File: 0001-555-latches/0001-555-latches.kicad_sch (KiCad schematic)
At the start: 33 parts, among them J1 DC_IN, J2 ASTBL_OUT, J3 BSTBL_OUT, J4 MSTBL_OUT, SW1 SW_Push, SW2 SW_Push, SW3 SW_Push, U1 NE555P, U2 NE555P, U3 NE555P

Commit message: footprints
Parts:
- C1, C2, C3, C5: footprint (none) -> Capacitor_THT:C_Rect_L7.0mm_W3.5mm_P5.00mm
- C4: footprint (none) -> Capacitor_THT:CP_Radial_D5.0mm_P2.00mm
- D1, D2, D3: footprint (none) -> LED_THT:LED_D5.0mm
- J1, J2, J3, J4: footprint (none) -> TerminalBlock_MetzConnect:TerminalBlock_MetzConnect_Type059_RT06302HBWC_1x02_P3.50mm_Horizontal
- R1, R10, R11, R12, R2, R3, R4, R5, R6, R7, R8, R9: footprint (none) -> Resistor_THT:R_Axial_DIN0207_L6.3mm_D2.5mm_P7.62mm_Horizontal
- RV1, RV2, RV3: footprint (none) -> Potentiometer_THT:Potentiometer_Runtron_RM-065_Vertical
- SW1, SW2, SW3: footprint (none) -> Button_Switch_THT:SW_PUSH_6mm_H4.3mm
- U1, U2, U3: footprint (none) -> Package_DIP:DIP-8_W7.62mm_Socket_LongPads
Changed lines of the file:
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@@
 			)
 		)
-		(property "Footprint" ""
+		(property "Footprint" "Button_Switch_THT:SW_PUSH_6mm_H4.3mm"
 			(at 116.84 76.2 0)
 			(effects
@@
 			)
 		)
-		(property "Footprint" ""
+		(property "Footprint" "LED_THT:LED_D5.0mm"
 			(at 78.74 92.71 0)
 			(effects
@@
 			)
 		)
-		(property "Footprint" ""
+		(property "Footprint" "Capacitor_THT:C_Rect_L7.0mm_W3.5mm_P5.00mm"
 			(at 135.5852 99.06 0)
 			(effects
@@
 			)
 		)
-		(property "Footprint" ""
+		(property "Footprint" "Resistor_THT:R_Axial_DIN0207_L6.3mm_D2.5mm_P7.62mm_Horizontal"
 			(at 132.842 34.29 90)
 			(effects
@@
 			)
 		)
-		(property "Footprint" ""
+		(property "Footprint" "Resistor_THT:R_Axial_DIN0207_L6.3mm_D2.5mm_P7.62mm_Horizontal"
 			(at 85.09 72.898 90)
 			(effects
@@
 			)
 		)
-		(property "Footprint" ""
+		(property "Footprint" "Resistor_THT:R_Axial_DIN0207_L6.3mm_D2.5mm_P7.62mm_Horizontal"
 			(at 196.342 34.29 90)
 			(effects
@@
 			)
 		)
-		(property "Footprint" ""
+		(property "Footprint" "Capacitor_THT:C_Rect_L7.0mm_W3.5mm_P5.00mm"
 			(at 211.7852 99.06 0)
 			(effects
@@
 			)
 		)
-		(property "Footprint" ""
+		(property "Footprint" "TerminalBlock_MetzConnect:TerminalBlock_MetzConnect_Type059_RT06302HBWC_1x02_P3.50mm_Horizontal"
 			(at 116.84 134.62 0)
 			(effects
@@
 			)
 		)
-		(property "Footprint" ""
+		(property "Footprint" "Package_DIP:DIP-8_W7.62mm_Socket_LongPads"
 			(at 74.93 86.36 0)
 			(effects
@@
 			)
 		)
-		(property "Footprint" ""
+		(property "Footprint" "Resistor_THT:R_Axial_DIN0207_L6.3mm_D2.5mm_P7.62mm_Horizontal"
 			(at 252.222 80.01 90)
 			(effects
@@
 			)
 		)
-		(property "Footprint" ""
+		(property "Footprint" "Button_Switch_THT:SW_PUSH_6mm_H4.3mm"
 			(at 116.84 53.34 0)
 			(effects
@@
 			)
 		)
-		(property "Footprint" ""
+		(property "Footprint" "Capacitor_THT:C_Rect_L7.0mm_W3.5mm_P5.00mm"
 			(at 39.0652 99.06 0)
 			(effects
@@
 			)
 		)
-		(property "Footprint" ""
+		(property "Footprint" "Resistor_THT:R_Axial_DIN0207_L6.3mm_D2.5mm_P7.62mm_Horizontal"
 			(at 239.522 34.29 90)
 			(effects
@@
 			)
 		)
-		(property "Datasheet" "~"
+		(property "Datasheet" ""
 			(at 241.3 34.29 0)
 			(effects
@@
 			)
 		)
-		(property "Footprint" ""
+		(property "Footprint" "Potentiometer_THT:Potentiometer_Runtron_RM-065_Vertical"
 			(at 241.3 46.99 0)
 			(effects
@@
 			)
 		)
-		(property "Footprint" ""
+		(property "Footprint" "Package_DIP:DIP-8_W7.62mm_Socket_LongPads"
 			(at 166.37 86.36 0)
 			(effects
@@
 			)
 		)
-		(property "Footprint" ""
+		(property "Footprint" "Button_Switch_THT:SW_PUSH_6mm_H4.3mm"
 			(at 193.04 81.28 0)
 			(effects
@@
 			)
 		)
-		(property "Footprint" ""
+		(property "Footprint" "Resistor_THT:R_Axial_DIN0207_L6.3mm_D2.5mm_P7.62mm_Horizontal"
 			(at 173.99 72.898 90)
 			(effects
@@
 			)
 		)
-		(property "Footprint" ""
+		(property "Footprint" "Potentiometer_THT:Potentiometer_Runtron_RM-065_Vertical"
 			(at 27.94 52.07 0)
 			(effects
@@
 			)
 		)
-		(property "Footprint" ""
+		(property "Footprint" "Package_DIP:DIP-8_W7.62mm_Socket_LongPads"
 			(at 242.57 86.36 0)
 			(effects
@@
 			)
 		)
-		(property "Footprint" ""
+		(property "Footprint" "TerminalBlock_MetzConnect:TerminalBlock_MetzConnect_Type059_RT06302HBWC_1x02_P3.50mm_Horizontal"
 			(at 157.48 134.62 0)
 			(effects
@@
 			)
 		)
-		(property "Footprint" ""
+		(property "Footprint" "Resistor_THT:R_Axial_DIN0207_L6.3mm_D2.5mm_P7.62mm_Horizontal"
 			(at 122.682 34.29 90)
 			(effects
@@
 			)
 		)
-		(property "Footprint" ""
+		(property "Footprint" "Capacitor_THT:C_Rect_L7.0mm_W3.5mm_P5.00mm"
 			(at 28.9052 99.06 0)
 			(effects
@@
 			)
 		)
-		(property "Footprint" ""
+		(property "Footprint" "Capacitor_THT:CP_Radial_D5.0mm_P2.00mm"
 			(at 242.2652 99.06 0)
 			(effects
@@
 			)
 		)
-		(property "Footprint" ""
+		(property "Footprint" "TerminalBlock_MetzConnect:TerminalBlock_MetzConnect_Type059_RT06302HBWC_1x02_P3.50mm_Horizontal"
 			(at 40.64 134.62 0)
 			(effects
@@
 			)
 		)
-		(property "Footprint" ""
+		(property "Footprint" "TerminalBlock_MetzConnect:TerminalBlock_MetzConnect_Type059_RT06302HBWC_1x02_P3.50mm_Horizontal"
 			(at 76.2 134.62 0)
 			(effects
@@
 			)
 		)
-		(property "Footprint" ""
+		(property "Footprint" "Resistor_THT:R_Axial_DIN0207_L6.3mm_D2.5mm_P7.62mm_Horizontal"
 			(at 76.962 80.01 90)
 			(effects
@@
 			)
 		)
-		(property "Footprint" ""
+		(property "Footprint" "LED_THT:LED_D5.0mm"
 			(at 254 92.71 0)
 			(effects
@@
 			)
 		)
-		(property "Footprint" ""
+		(property "Footprint" "Resistor_THT:R_Axial_DIN0207_L6.3mm_D2.5mm_P7.62mm_Horizontal"
 			(at 26.162 29.21 90)
 			(effects
@@
 			)
 		)
-		(property "Footprint" ""
+		(property "Footprint" "Potentiometer_THT:Potentiometer_Runtron_RM-065_Vertical"
 			(at 27.94 39.37 0)
 			(effects
@@
 			)
 		)
-		(property "Footprint" ""
+		(property "Footprint" "LED_THT:LED_D5.0mm"
 			(at 167.64 92.71 0)
 			(effects
@@
 			)
 		)
-		(property "Footprint" ""
+		(property "Footprint" "Resistor_THT:R_Axial_DIN0207_L6.3mm_D2.5mm_P7.62mm_Horizontal"
 			(at 260.35 72.898 90)
 			(effects
@@
 			)
 		)
-		(property "Footprint" ""
+		(property "Footprint" "Resistor_THT:R_Axial_DIN0207_L6.3mm_D2.5mm_P7.62mm_Horizontal"
 			(at 26.162 64.77 90)
 			(effects
@@
 			)
 		)
-		(property "Footprint" ""
+		(property "Footprint" "Resistor_THT:R_Axial_DIN0207_L6.3mm_D2.5mm_P7.62mm_Horizontal"
 			(at 165.862 80.01 90)
 			(effects

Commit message: Fix typo
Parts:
- D3: value YELLO -> YELLOW
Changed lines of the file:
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@@
 			)
 		)
-		(property "Value" "YELLO"
+		(property "Value" "YELLOW"
 			(at 257.81 95.5674 90)
 			(effects

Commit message: First PCB drafts
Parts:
- J1, J2, J3, J4: footprint TerminalBlock_MetzConnect:TerminalBlock_MetzConnect_Type059_RT06302HBWC_1x02_P3.50mm_Horizontal -> TerminalBlock_4Ucon:TerminalBlock_4Ucon_1x02_P3.50mm_Horizontal
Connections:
- net at R6.2: now also RV3.3; no longer RV3.1
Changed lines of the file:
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@@
 			)
 		)
-		(property "Footprint" "TerminalBlock_MetzConnect:TerminalBlock_MetzConnect_Type059_RT06302HBWC_1x02_P3.50mm_Horizontal"
+		(property "Footprint" "TerminalBlock_4Ucon:TerminalBlock_4Ucon_1x02_P3.50mm_Horizontal"
 			(at 116.84 134.62 0)
 			(effects
@@
 		(lib_id "Device:R_Potentiometer")
 		(at 241.3 46.99 0)
-		(unit 1)
-		(exclude_from_sim no)
-		(in_bom yes)
-		(on_board yes)
-		(dnp no)
-		(fields_autoplaced yes)
+		(mirror x)
+		(unit 1)
+		(exclude_from_sim no)
+		(in_bom yes)
+		(on_board yes)
+		(dnp no)
 		(property "Reference" "RV3"
-			(at 238.76 45.7199 0)
+			(at 238.76 48.2601 0)
 			(effects
 				(font
@@
 		)
 		(property "Value" "1M"
-			(at 238.76 48.2599 0)
+			(at 238.76 45.7201 0)
 			(effects
 				(font
@@
 			)
 		)
-		(property "Footprint" "TerminalBlock_MetzConnect:TerminalBlock_MetzConnect_Type059_RT06302HBWC_1x02_P3.50mm_Horizontal"
+		(property "Footprint" "TerminalBlock_4Ucon:TerminalBlock_4Ucon_1x02_P3.50mm_Horizontal"
 			(at 157.48 134.62 0)
 			(effects
@@
 			)
 		)
-		(property "Footprint" "TerminalBlock_MetzConnect:TerminalBlock_MetzConnect_Type059_RT06302HBWC_1x02_P3.50mm_Horizontal"
+		(property "Footprint" "TerminalBlock_4Ucon:TerminalBlock_4Ucon_1x02_P3.50mm_Horizontal"
 			(at 40.64 134.62 0)
 			(effects
@@
 			)
 		)
-		(property "Footprint" "TerminalBlock_MetzConnect:TerminalBlock_MetzConnect_Type059_RT06302HBWC_1x02_P3.50mm_Horizontal"
+		(property "Footprint" "TerminalBlock_4Ucon:TerminalBlock_4Ucon_1x02_P3.50mm_Horizontal"
 			(at 76.2 134.62 0)
 			(effects

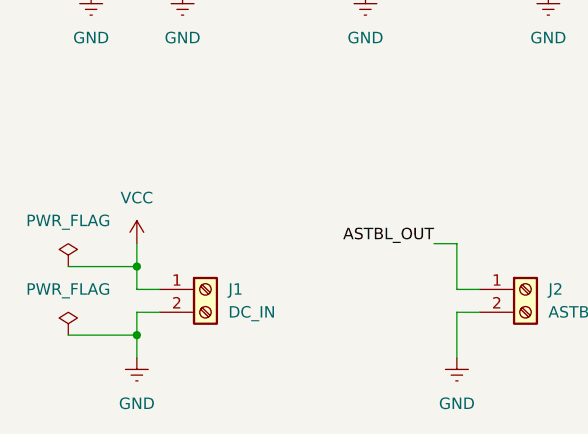
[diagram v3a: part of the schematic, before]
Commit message: Replace DC_IN screw connector with DC jack
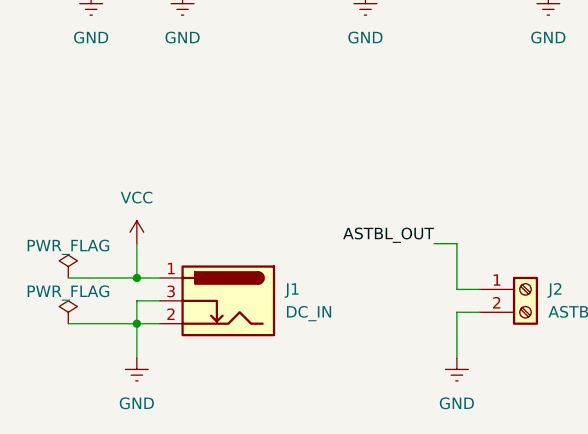
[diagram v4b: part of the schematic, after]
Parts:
- removed J1: DC_IN, TerminalBlock_4Ucon:TerminalBlock_4Ucon_1x02_P3.50mm_Horizontal, symbol Connector:Screw_Terminal_01x02
- added J1: DC_IN, Connector_BarrelJack:BarrelJack_Horizontal, symbol Connector:Barrel_Jack_Switch
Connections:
- net GND: now also J1.2, J1.3
- net VCC: now also J1.1
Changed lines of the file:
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@@
 	)
 	(junction
-		(at 198.12 71.12)
+		(at 33.02 133.35)
 		(diameter 0)
 		(color 0 0 0 0)
 	)
 	(junction
-		(at 33.02 139.7)
+		(at 198.12 71.12)
 		(diameter 0)
 		(color 0 0 0 0)
@@
 	)
 	(junction
-		(at 33.02 132.08)
+		(at 78.74 71.12)
 		(diameter 0)
 		(color 0 0 0 0)
 	)
 	(junction
-		(at 78.74 71.12)
+		(at 109.22 81.28)
 		(diameter 0)
 		(color 0 0 0 0)
 	)
 	(junction
-		(at 109.22 81.28)
+		(at 33.02 138.43)
 		(diameter 0)
 		(color 0 0 0 0)
@@
 	(wire
 		(pts
-			(xy 33.02 139.7) (xy 33.02 137.16)
-		)
-		(stroke
-			(width 0)
-			(type default)
-		)
-	)
-	(wire
-		(pts
 			(xy 149.86 142.24) (xy 149.86 137.16)
 		)
@@
 	(wire
 		(pts
-			(xy 241.3 99.06) (xy 241.3 101.6)
+			(xy 33.02 135.89) (xy 33.02 138.43)
 		)
 		(stroke
@@
 	(wire
 		(pts
-			(xy 149.86 22.86) (xy 149.86 66.04)
+			(xy 241.3 99.06) (xy 241.3 101.6)
 		)
 		(stroke
@@
 	(wire
 		(pts
-			(xy 27.94 88.9) (xy 73.66 88.9)
+			(xy 149.86 22.86) (xy 149.86 66.04)
 		)
 		(stroke
@@
 	(wire
 		(pts
-			(xy 33.02 134.62) (xy 35.56 134.62)
+			(xy 27.94 88.9) (xy 73.66 88.9)
 		)
 		(stroke
@@
 	(wire
 		(pts
-			(xy 33.02 142.24) (xy 33.02 139.7)
+			(xy 33.02 138.43) (xy 33.02 142.24)
 		)
 		(stroke
@@
 	(wire
 		(pts
-			(xy 33.02 137.16) (xy 35.56 137.16)
-		)
-		(stroke
-			(width 0)
-			(type default)
-		)
-	)
-	(wire
-		(pts
 			(xy 68.58 134.62) (xy 71.12 134.62)
 		)
@@
 	(wire
 		(pts
-			(xy 25.4 132.08) (xy 33.02 132.08)
+			(xy 25.4 133.35) (xy 33.02 133.35)
 		)
 		(stroke
@@
 	(wire
 		(pts
-			(xy 33.02 132.08) (xy 33.02 134.62)
+			(xy 210.82 99.06) (xy 210.82 101.6)
 		)
 		(stroke
@@
 	(wire
 		(pts
-			(xy 210.82 99.06) (xy 210.82 101.6)
+			(xy 254 83.82) (xy 254 88.9)
 		)
 		(stroke
@@
 	(wire
 		(pts
-			(xy 254 83.82) (xy 254 88.9)
+			(xy 78.74 71.12) (xy 78.74 76.2)
 		)
 		(stroke
@@
 	(wire
 		(pts
-			(xy 78.74 71.12) (xy 78.74 76.2)
+			(xy 254 96.52) (xy 254 101.6)
 		)
 		(stroke
@@
 	(wire
 		(pts
-			(xy 254 96.52) (xy 254 101.6)
+			(xy 167.64 96.52) (xy 167.64 101.6)
 		)
 		(stroke
@@
 	(wire
 		(pts
-			(xy 167.64 96.52) (xy 167.64 101.6)
+			(xy 35.56 135.89) (xy 33.02 135.89)
 		)
 		(stroke
@@
 	(wire
 		(pts
-			(xy 25.4 139.7) (xy 33.02 139.7)
+			(xy 35.56 133.35) (xy 33.02 133.35)
+		)
+		(stroke
+			(width 0)
+			(type default)
+		)
+	)
+	(wire
+		(pts
+			(xy 25.4 138.43) (xy 33.02 138.43)
 		)
 		(stroke
@@
 	(wire
 		(pts
-			(xy 33.02 129.54) (xy 33.02 132.08)
+			(xy 121.92 81.28) (xy 124.46 81.28)
 		)
 		(stroke
@@
 	(wire
 		(pts
-			(xy 121.92 81.28) (xy 124.46 81.28)
+			(xy 35.56 138.43) (xy 33.02 138.43)
 		)
 		(stroke
@@
 	(wire
 		(pts
+			(xy 33.02 129.54) (xy 33.02 133.35)
+		)
+		(stroke
+			(width 0)
+			(type default)
+		)
+	)
+	(wire
+		(pts
 			(xy 31.75 39.37) (xy 35.56 39.37)
 		)
@@
 	)
 	(symbol
+		(lib_id "Connector:Barrel_Jack_Switch")
+		(at 43.18 135.89 0)
+		(mirror y)
+		(unit 1)
+		(exclude_from_sim no)
+		(in_bom yes)
+		(on_board yes)
+		(dnp no)
+		(fields_autoplaced yes)
+		(property "Reference" "J1"
+			(at 49.53 134.6199 0)
+			(effects
+				(font
+					(size 1.27 1.27)
+				)
+				(justify right)
+			)
+		)
+		(property "Value" "DC_IN"
+			(at 49.53 137.1599 0)
+			(effects
+				(font
+					(size 1.27 1.27)
+				)
+				(justify right)
+			)
+		)
+		(property "Footprint" "Connector_BarrelJack:BarrelJack_Horizontal"
+			(at 41.91 136.906 0)
+			(effects
+				(font
+					(size 1.27 1.27)
+				)
+				(hide yes)
+			)
+		)
+		(property "Datasheet" "~"
+			(at 41.91 136.906 0)
+			(effects
+				(font
+					(size 1.27 1.27)
+				)
+				(hide yes)
+			)
+		)
+		(property "Description" "DC Barrel Jack with an internal switch"
+			(at 43.18 135.89 0)
+			(effects
+				(font
+					(size 1.27 1.27)
+				)
+				(hide yes)
+			)
+		)
+		(pin "2"
+		)
+		(pin "3"
+		)
+		(pin "1"
+		)
+		(instances
+			(project ""
+				(path "/11cec59d-a989-4950-8b21-3f1fb45ca1cc"
+					(reference "J1")
+					(unit 1)
+				)
+			)
+		)
+	)
+	(symbol
 		(lib_id "Switch:SW_Push")
 		(at 116.84 81.28 0)
@@
 	(symbol
 		(lib_id "power:PWR_FLAG")
-		(at 25.4 132.08 0)
+		(at 25.4 133.35 0)
 		(unit 1)
 		(exclude_from_sim no)
@@
 		(on_board yes)
 		(dnp no)
-		(fields_autoplaced yes)
 		(property "Reference" "#FLG01"
-			(at 25.4 130.175 0)
+			(at 25.4 131.445 0)
 			(effects
 				(font
@@
 		)
 		(property "Value" "PWR_FLAG"
-			(at 25.4 127 0)
+			(at 25.4 129.794 0)
 			(effects
 				(font
@@
 		)
 		(property "Footprint" ""
-			(at 25.4 132.08 0)
+			(at 25.4 133.35 0)
 			(effects
 				(font
@@
 		)
 		(property "Datasheet" "~"
-			(at 25.4 132.08 0)
+			(at 25.4 133.35 0)
 			(effects
 				(font
@@
 		)
 		(property "Description" "Special symbol for telling ERC where power comes from"
-			(at 25.4 132.08 0)
+			(at 25.4 133.35 0)
 			(effects
 				(font
@@
 	(symbol
 		(lib_id "Connector:Screw_Terminal_01x02")
-		(at 40.64 134.62 0)
-		(unit 1)
-		(exclude_from_sim no)
-		(in_bom yes)
-		(on_board yes)
-		(dnp no)
-		(fields_autoplaced yes)
-		(property "Reference" "J1"
-			(at 43.18 134.6199 0)
-			(effects
-				(font
-					(size 1.27 1.27)
-				)
-				(justify left)
-			)
-		)
-		(property "Value" "DC_IN"
-			(at 43.18 137.1599 0)
-			(effects
-				(font
-					(size 1.27 1.27)
-				)
-				(justify left)
-			)
-		)
-		(property "Footprint" "TerminalBlock_4Ucon:TerminalBlock_4Ucon_1x02_P3.50mm_Horizontal"
-			(at 40.64 134.62 0)
-			(effects
-				(font
-					(size 1.27 1.27)
-				)
-				(hide yes)
-			)
-		)
-		(property "Datasheet" "~"
-			(at 40.64 134.62 0)
-			(effects
-				(font
-					(size 1.27 1.27)
-				)
-				(hide yes)
-			)
-		)
-		(property "Description" "Generic screw terminal, single row, 01x02, script generated (kicad-library-utils/schlib/autogen/connector/)"
-			(at 40.64 134.62 0)
-			(effects
-				(font
-					(size 1.27 1.27)
-				)
-				(hide yes)
-			)
-		)
-		(pin "2"
-		)
-		(pin "1"
-		)
-		(instances
-			(project ""
-				(path "/11cec59d-a989-4950-8b21-3f1fb45ca1cc"
-					(reference "J1")
-					(unit 1)
-				)
-			)
-		)
-	)
-	(symbol
-		(lib_id "Connector:Screw_Terminal_01x02")
 		(at 76.2 134.62 0)
 		(unit 1)
@@
 	(symbol
 		(lib_id "power:PWR_FLAG")
-		(at 25.4 139.7 0)
+		(at 25.4 138.43 0)
 		(unit 1)
 		(exclude_from_sim no)
@@
 		(on_board yes)
 		(dnp no)
-		(fields_autoplaced yes)
 		(property "Reference" "#FLG02"
-			(at 25.4 137.795 0)
+			(at 25.4 136.525 0)
 			(effects
 				(font
@@
 		)
 		(property "Value" "PWR_FLAG"
-			(at 25.4 134.62 0)
+			(at 25.4 134.874 0)
 			(effects
 				(font
@@
 		)
 		(property "Footprint" ""
-			(at 25.4 139.7 0)
+			(at 25.4 138.43 0)
 			(effects
 				(font
@@
 		)
 		(property "Datasheet" "~"
-			(at 25.4 139.7 0)
+			(at 25.4 138.43 0)
 			(effects
 				(font
@@
 		)
 		(property "Description" "Special symbol for telling ERC where power comes from"
-			(at 25.4 139.7 0)
+			(at 25.4 138.43 0)
 			(effects
 				(font
